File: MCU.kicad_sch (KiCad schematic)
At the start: 30 parts, among them J1 USB_B_Micro, J2 Conn_01x02, J4 Debugger Pins, J6 GPIO, U1 NCP1117-3.3_SOT223, U2 W25Q128JVS, U3 RP2040, Y1 ABLS-12.000MHZ-B4-T

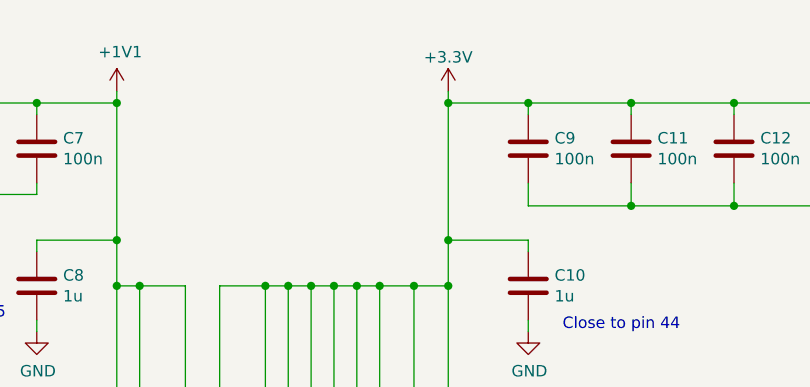
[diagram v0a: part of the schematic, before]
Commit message: added nets to high level circuit
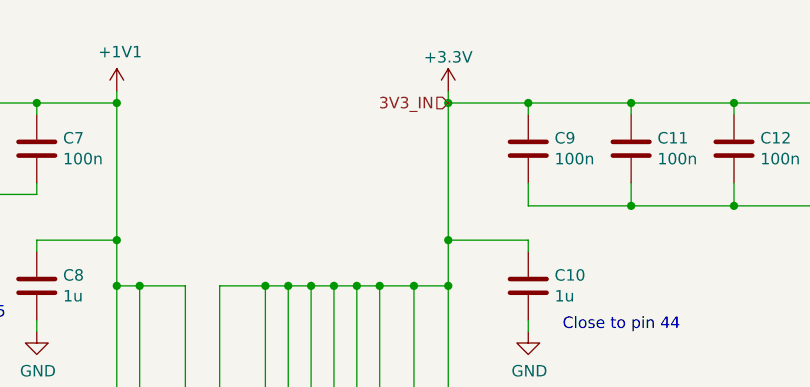
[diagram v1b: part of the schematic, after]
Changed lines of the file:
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@@
     (effects (font (size 1.27 1.27)) (justify left))
+  )
+  (hierarchical_label "3V3_IN" (shape input) (at 181.61 27.94 180) (fields_autoplaced)
+    (effects (font (size 1.27 1.27)) (justify right))
   )
   (hierarchical_label "OUT_H2" (shape output) (at 212.09 127 0) (fields_autoplaced)
